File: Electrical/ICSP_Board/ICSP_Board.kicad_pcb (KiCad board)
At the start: 2 copper layers, 74 x 54 mm, 46 parts, among them J1 card_edge_6p, J2 card_edge_6p, J3 card_edge_6p, J4 card_edge_6p, J5 card_edge_6p, J6 card_edge_6p, Q1 BC850, Q2 BC850, Q3 BC850, Q4 BC850, Q5 BC850, Q6 BC850, SW1 SW_Push, U1 ULN2003A

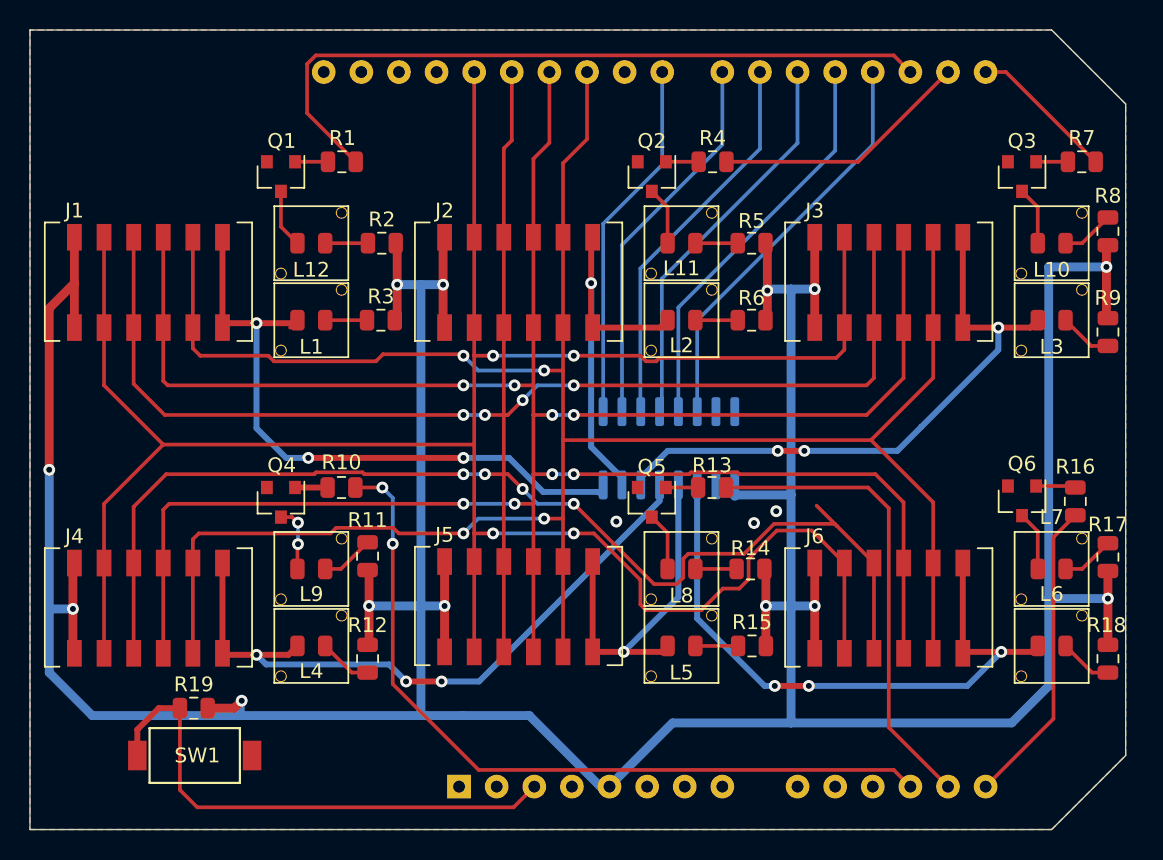
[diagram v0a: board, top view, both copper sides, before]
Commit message: Fixed hole size on ICSP board.
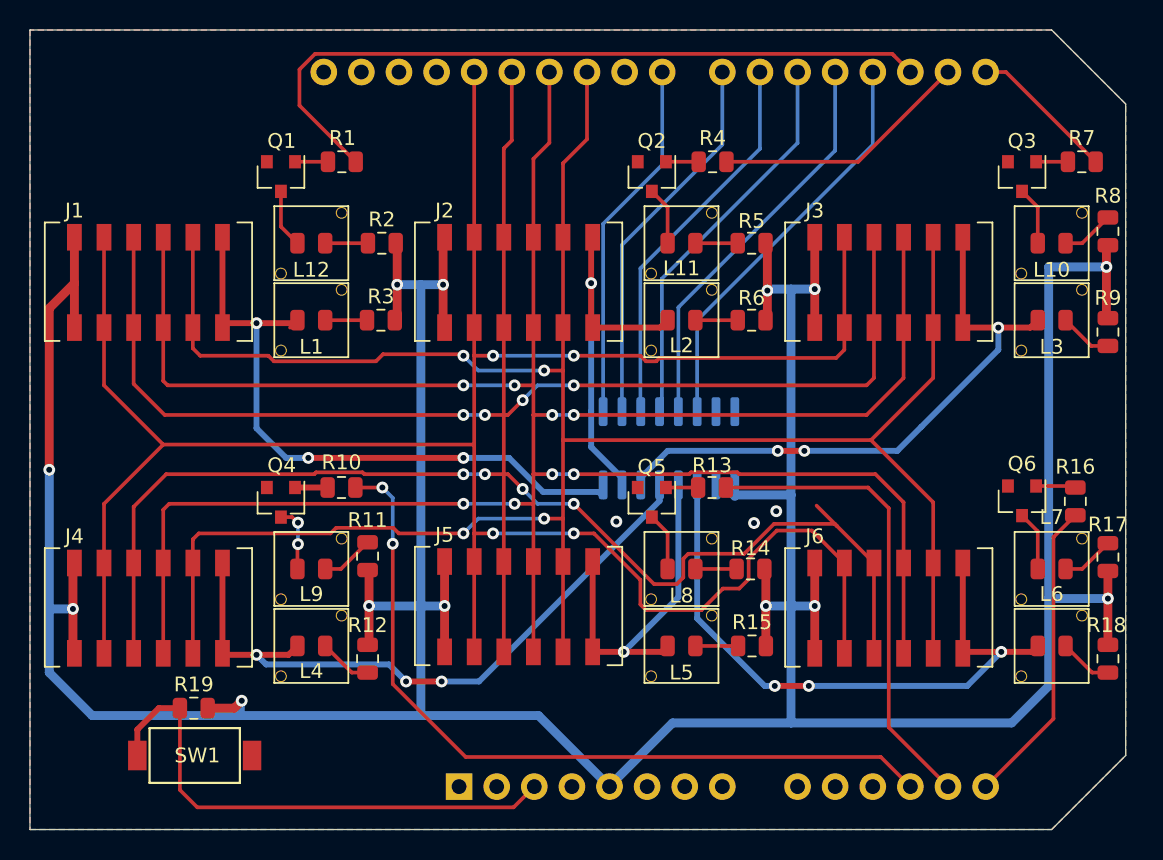
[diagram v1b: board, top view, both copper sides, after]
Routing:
- net +5V: track 286.6 -> 287.2 mm
- net Net-(A1-Pad17): track 49.4 -> 50.0 mm

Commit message: Initial ICSP housing rough cut.
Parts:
- J1, J2, J3, J4, J5, J6: value card_edge_6p -> AVX 009159006551906
- renumbered L12 to L1, L5 to L10, L7 to L11, L6 to L12, L1 to L2, L11 to L3, L2 to L4, L10 to L5, L3 to L6, L9 to L7, L4 to L8, L8 to L9
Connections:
- A1 pad 8: Net-(A1-Pad8) -> VCC
- J1 pad 1: +5V -> VCC
- J2 pad 1: +5V -> VCC
- J3 pad 1: +5V -> VCC
- J4 pad 1: +5V -> VCC
- J5 pad 1: +5V -> VCC
- J6 pad 1: +5V -> VCC
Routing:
- net VCC: track 0.00 -> 193.7 mm, vias 0 -> 7
- net +5V: track 287.2 -> 201.5 mm, vias 13 -> 7
- net /MISO: track 186.6 -> 184.6 mm
